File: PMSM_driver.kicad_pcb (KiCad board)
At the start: 2 copper layers, 86 x 76 mm, 86 parts, among them J1 22-23-2021, J2 Screw_Terminal_Power, J3 Screw_Terminal_1, J4 Screw_Terminal_2, J5 Screw_Terminal_3, J6 Screw_Terminal_Logic, J7 302-S101, Q1 IRFH8334, Q2 IRFH8334, Q3 IRFH8334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

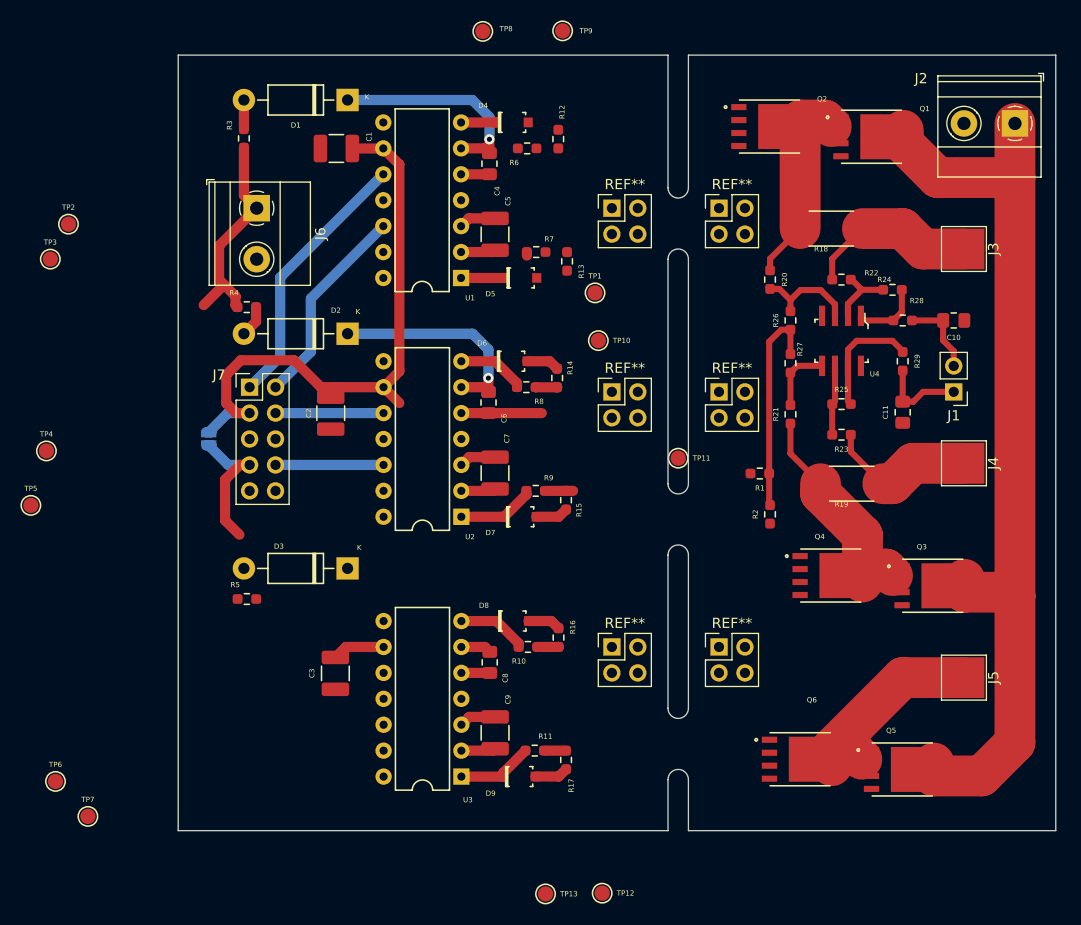
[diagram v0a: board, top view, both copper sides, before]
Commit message: [PCB]: Logic - Power boards tracing
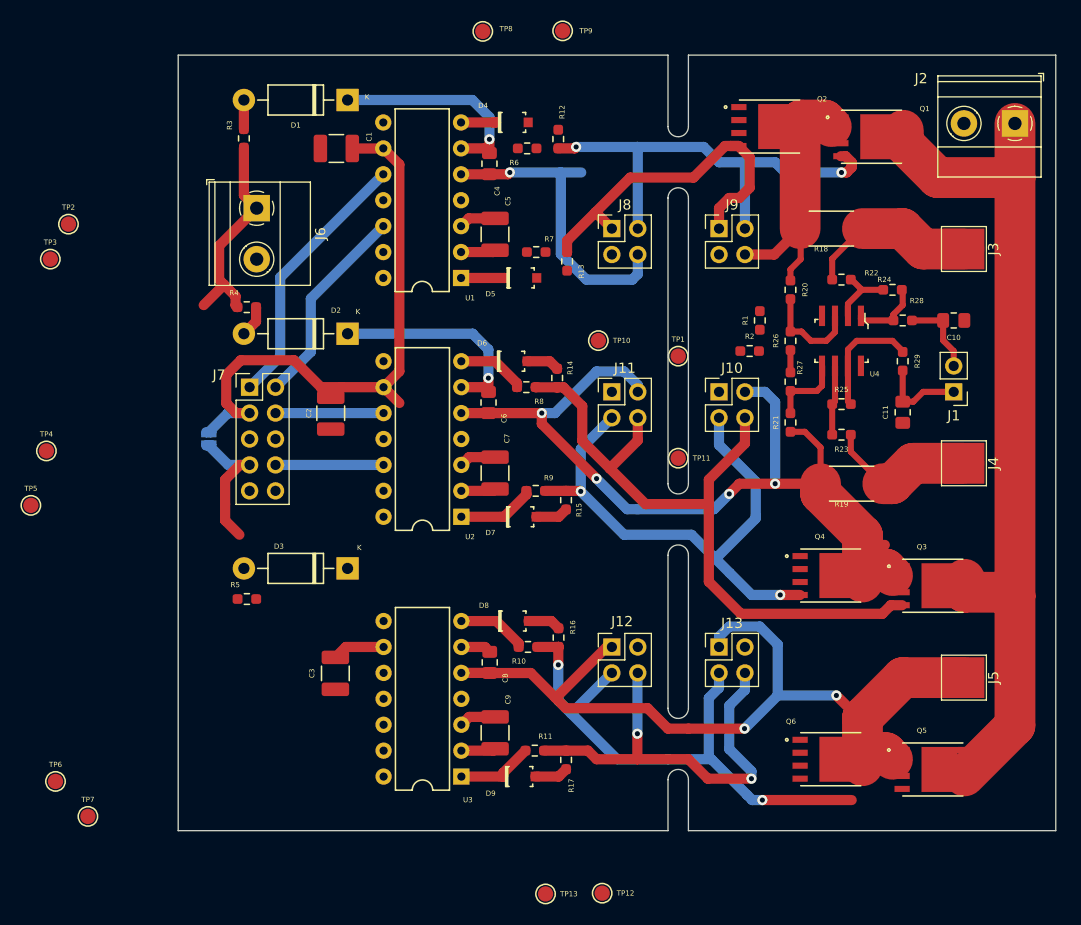
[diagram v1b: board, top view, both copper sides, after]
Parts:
- removed REF** (x6): PinHeader_1, Connector_PinHeader_2.54mm:PinHeader_2x02_P2.54mm_Vertical
- added J10: Conn21, Connector_PinHeader_2.54mm:PinHeader_2x02_P2.54mm_Vertical, F.Cu at (151.0, 84.0)
- added J11: Conn22, Connector_PinHeader_2.54mm:PinHeader_2x02_P2.54mm_Vertical, F.Cu at (140.5, 84.0)
- added J12: Conn31, Connector_PinHeader_2.54mm:PinHeader_2x02_P2.54mm_Vertical, F.Cu at (140.5, 109.0)
- added J13: Conn32, Connector_PinHeader_2.54mm:PinHeader_2x02_P2.54mm_Vertical, F.Cu at (151.0, 109.0)
- added J8: Conn11, Connector_PinHeader_2.54mm:PinHeader_2x02_P2.54mm_Vertical, F.Cu at (140.5, 68.0)
- added J9: Conn12, Connector_PinHeader_2.54mm:PinHeader_2x02_P2.54mm_Vertical, F.Cu at (151.0, 68.0)
- moved R2 16.1 mm to (154.0, 80.0), turned to 0 degrees
- moved R1 15.0 mm to (155.0, 77.0), turned to 90 degrees
- moved TP1 10.2 mm to (147.0, 80.5)
- moved Q5 3.00 mm to (172.0, 121.0)
- moved Q6 3.00 mm to (162.0, 120.0)
- moved R20 2.24 mm to (158.0, 74.0)
- moved R26 2.00 mm to (158.0, 79.0)
- moved R27 1.80 mm to (158.0, 83.0)
- moved R21 0.80 mm to (158.0, 87.0)
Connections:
- net Net-(Q1-Pad4) renamed /Q1_G
- net Net-(Q2-Pad4) renamed /Q2_G
- net Net-(Q3-Pad4) renamed /Q3_G
- net Net-(Q4-Pad4) renamed /Q4_G
- net Net-(Q5-Pad4) renamed /Q5_G
- net Net-(Q6-Pad4) renamed /Q6_G
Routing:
- net /Q3_G: track 2.15 -> 68.0 mm
- net PHASE_3: track 23.5 -> 83.8 mm, vias 0 -> 2
- net /Q3_Q4: track 28.3 -> 87.5 mm, vias 0 -> 4
- net /Q5_G: track 2.09 -> 54.8 mm, vias 0 -> 2
- net /Q4_G: track 2.75 -> 54.6 mm, vias 0 -> 2
- net /Q1_G: track 0.00 -> 46.4 mm, vias 0 -> 2
- net /Q6_G: track 2.16 -> 41.8 mm, vias 0 -> 2
- net /Q2_G: track 0.00 -> 35.2 mm
- net /Q1_Q2: track 22.0 -> 56.4 mm, vias 0 -> 1
- net 1V65: track 21.0 -> 2.18 mm
- net +VDC: track 91.2 -> 86.0 mm
- net Net-(R21-Pad2): track 6.54 -> 7.44 mm
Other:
- outline, holes or cut-outs redrawn

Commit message: [DRC]: DRC checks were passed
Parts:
- removed the TP2 at (87.2, 67.6)
- removed the TP3 at (85.5, 71.0)
- removed the TP4 at (85.1, 89.8)
- removed the TP5 at (83.6, 95.1)
- removed the TP6 at (86.0, 122.2)
- removed the TP7 at (89.2, 125.6)
- J1: value 22-23-2021 -> 640456-3; footprint Connector_PinHeader_2.54mm:PinHeader_1x02_P2.54mm_Vertical -> Connector_PinHeader_2.54mm:PinHeader_1x03_P2.54mm_Vertical
- moved TP6 31.0 mm to (129.2, 103.9)
- moved TP3 19.6 mm to (132.2, 67.9)
- moved TP5 14.9 mm to (132.1, 91.4)
- moved TP1 10.5 mm to (155.0, 73.7)
- moved TP4 10.2 mm to (129.0, 78.3)
- moved TP7 9.92 mm to (129.8, 124.2)
- moved TP2 6.55 mm to (129.1, 55.1)
- moved J1 4.50 mm to (174.0, 79.5), turned to 0 degrees
- moved C10 1.02 mm to (174.0, 76.0)
- renumbered TP8 to TP2, TP9 to TP3, TP10 to TP4, TP11 to TP5, TP12 to TP6, TP13 to TP7
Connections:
- J1 pad 1: /CUR_OUT_2 -> /CUR_OUT_1
- J1 pad 2: /CUR_OUT_1 -> /CUR_OUT_2
- J10 pad 3: /Q4_G -> /Q3_G
- J10 pad 4: /Q3_G -> /Q4_G
- J11 pad 3: /Q4_G -> /Q3_G
- J11 pad 4: /Q3_G -> /Q4_G
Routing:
- net VCC: track 32.1 -> 144.2 mm, vias 0 -> 1
- net +3.3V: track 13.8 -> 106.4 mm, vias 0 -> 4
- net +VDC: track 86.0 -> 116.8 mm, vias 0 -> 1
- net /L3: track 0.00 -> 28.4 mm
- net VDD: track 65.3 -> 90.8 mm
- net /H3: track 0.00 -> 22.2 mm
- net Net-(C8-Pad1): track 2.98 -> 23.2 mm, vias 0 -> 1
- net /Q1_Q2: track 56.4 -> 75.8 mm, vias 1 -> 2
- net 1V65: track 2.18 -> 13.3 mm
- net Net-(D4-PadK): track 3.43 -> 9.38 mm
- net Net-(D5-PadK): track 4.27 -> 10.1 mm
- net /Q4_G: track 54.6 -> 60.4 mm
- net /Q5_G: track 54.8 -> 59.9 mm
- net /Q6_G: track 41.8 -> 46.5 mm
- net /Q2_G: track 35.2 -> 38.8 mm, vias 0 -> 2
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- added copper zone on B.Cu, net GND
- added copper zone on F.Cu, net GND

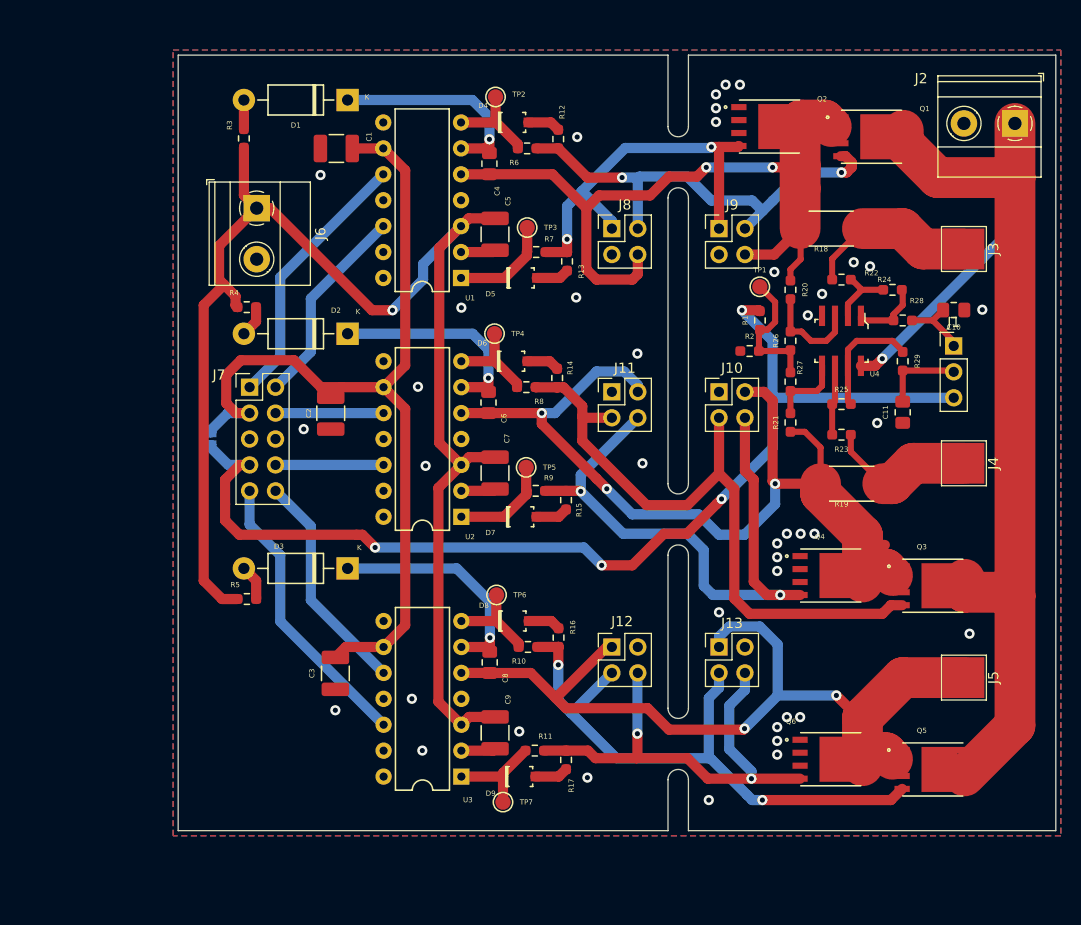
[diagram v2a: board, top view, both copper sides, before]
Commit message: [PCB]: JLCPCB constraints
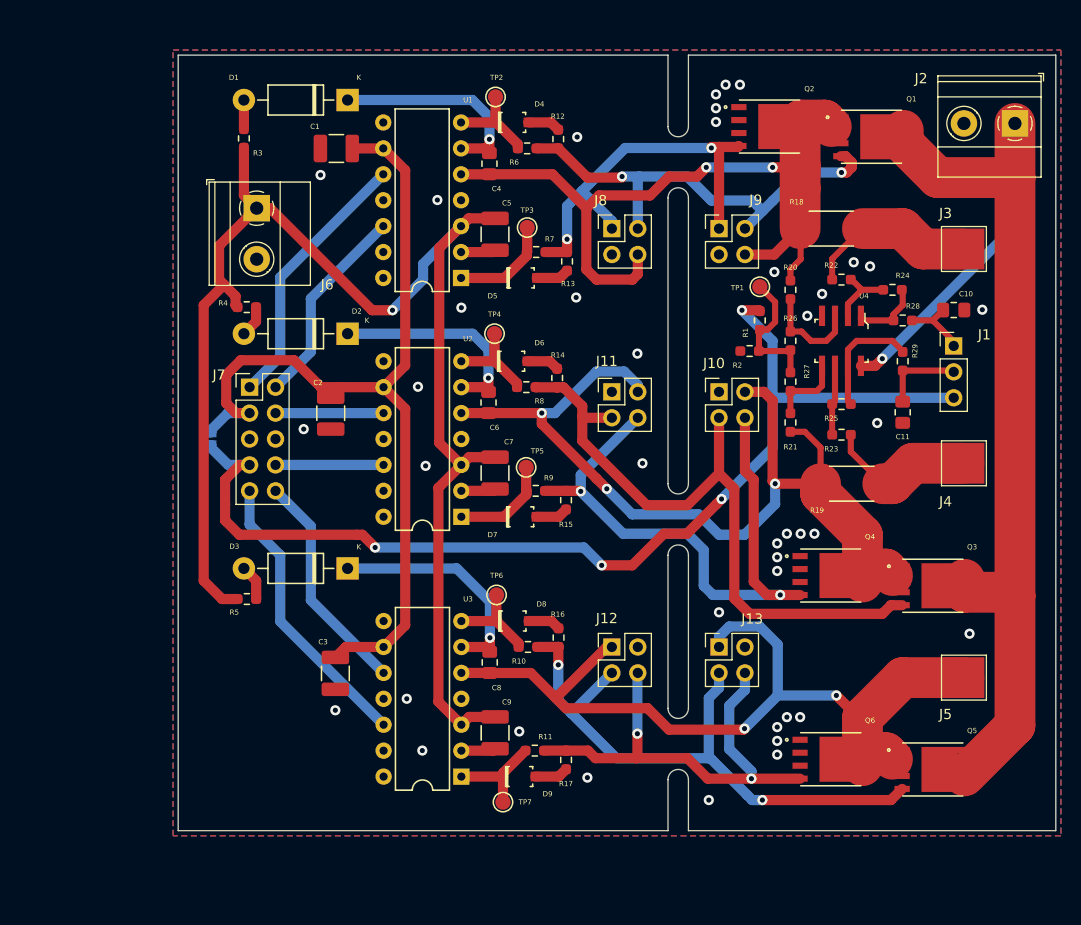
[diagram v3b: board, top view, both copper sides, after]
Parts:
- J1: value 640456-3 -> Current
- J3: value Screw_Terminal_1 -> Phase_1
- J4: value Screw_Terminal_2 -> Phase_2
- J5: value Screw_Terminal_3 -> Phase_3
- J7: value 302-S101 -> Interface
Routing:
- net /Q3_Q4: track 90.7 -> 89.6 mm
- net GND: vias 40 -> 41

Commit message: [PCB]: Power traces enlargement
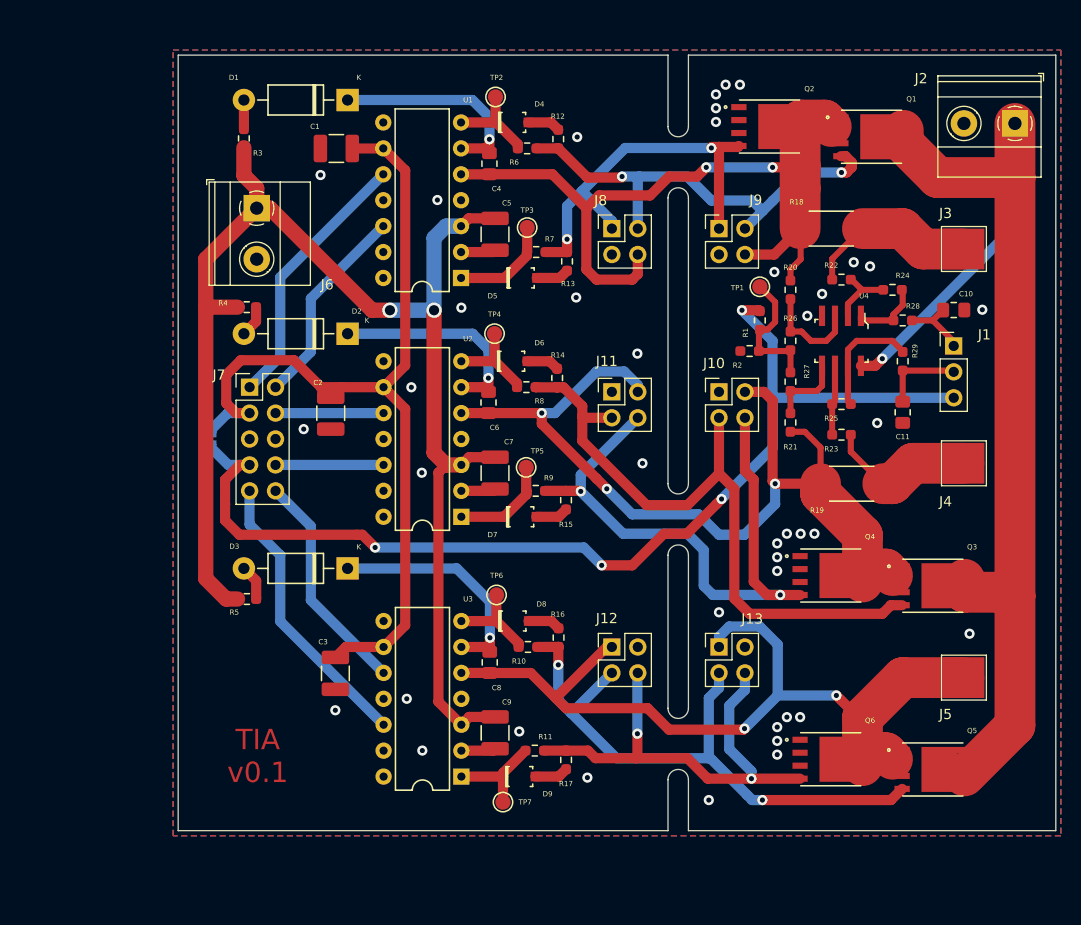
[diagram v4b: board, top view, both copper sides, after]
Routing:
- net VCC: track 144.2 -> 138.3 mm, vias 1 -> 2
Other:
- board text added: "TIA v0.1"
